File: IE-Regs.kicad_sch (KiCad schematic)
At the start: 15 parts, among them J40 Vin, J41 Gnd, U50 SPX3819M5-L-3-3, U60 SY8113BADC

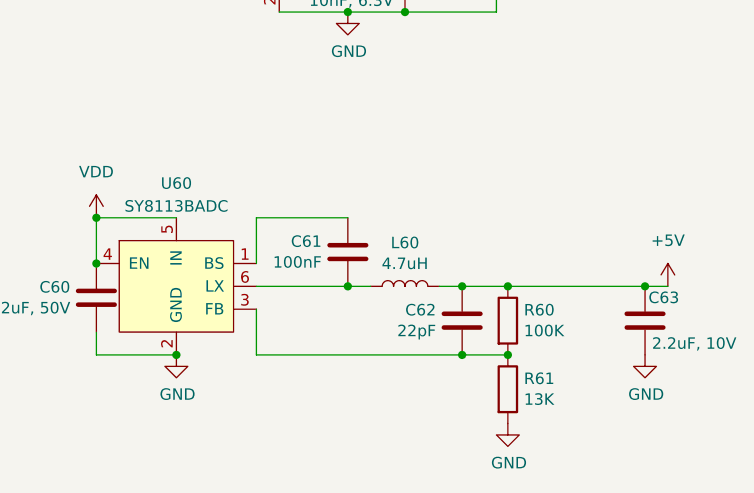
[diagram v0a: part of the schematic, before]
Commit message: initial copy from goldESC
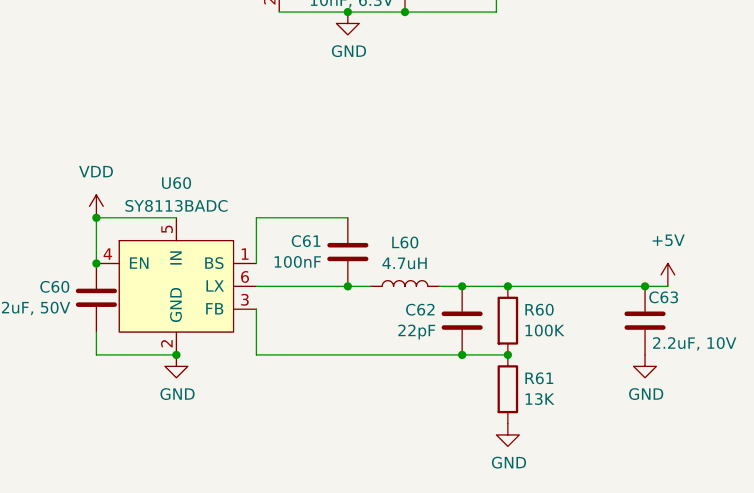
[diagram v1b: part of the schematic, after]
